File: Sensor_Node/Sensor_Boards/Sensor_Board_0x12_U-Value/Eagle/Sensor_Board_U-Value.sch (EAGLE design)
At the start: 25 parts, among them IC1 MCP3911A0-E/SS, IC2 4066D, J2 ARDUINO_ISP, U2 ATMEGA328P_TQFP, Y1 8MHZ

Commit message: Added WSN eagle library
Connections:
- removed net D11_MOSI: U2.PB3(MOSI/OC2)
- removed net D12_MISO: J2.MISO, J2.MOSI, U2.PB4(MISO)
- removed net D13_SCK: J2.SCK, U2.PB5(SCK)
- removed net N$16: U2.PD2(INT0)
- removed net N$20: U2.PD6(AIN0)
- removed net N$21: U2.PD7(AIN1)
- net ADCLK: now also U2.PD2(INT0)
- net AD_CS: now also U2.PD6(AIN0)
- net DATA_READY: now also U2.PD7(AIN1)
- net MISO: now also J2.MISO, U2.PB4(MISO)
- net MOSI: now also J2.MOSI, U2.PB3(MOSI/OC2)
- net SCK: now also J2.SCK, U2.PB5(SCK)
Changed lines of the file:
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@@
 <?xml version="1.0" encoding="utf-8"?>
 <!DOCTYPE eagle SYSTEM "eagle.dtd">
-<eagle version="7.6.0">
+<eagle version="8.2.2">
 <drawing>
 <settings>
@@
 <part name="NC10" library="wsn" deviceset="NC" device=""/>
 <part name="NC11" library="wsn" deviceset="NC" device=""/>
-<part name="NC12" library="wsn" deviceset="NC" device=""/>
 <part name="NC13" library="wsn" deviceset="NC" device=""/>
 <part name="NC14" library="wsn" deviceset="NC" device=""/>
 <part name="NC15" library="wsn" deviceset="NC" device=""/>
-<part name="NC16" library="wsn" deviceset="NC" device=""/>
-<part name="NC17" library="wsn" deviceset="NC" device=""/>
 <part name="NC18" library="wsn" deviceset="NC" device=""/>
 <part name="GND6" library="supply1" deviceset="GND" device=""/>
@@
 <instance part="NC10" gate="G$1" x="236.22" y="83.82"/>
 <instance part="NC11" gate="G$1" x="236.22" y="81.28"/>
-<instance part="NC12" gate="G$1" x="236.22" y="78.74"/>
 <instance part="NC13" gate="G$1" x="236.22" y="76.2"/>
 <instance part="NC14" gate="G$1" x="236.22" y="73.66"/>
 <instance part="NC15" gate="G$1" x="236.22" y="71.12"/>
-<instance part="NC16" gate="G$1" x="236.22" y="68.58"/>
-<instance part="NC17" gate="G$1" x="236.22" y="66.04"/>
 <instance part="NC18" gate="G$1" x="236.22" y="63.5"/>
 <instance part="GND6" gate="1" x="182.88" y="43.18"/>
@@
 <pinref part="IC1" gate="G$1" pin="SDO"/>
 </segment>
+<segment>
+<pinref part="U2" gate="U$1" pin="PB4(MISO)"/>
+<wire x1="236.22" y1="53.34" x2="233.68" y2="53.34" width="0.1524" layer="91"/>
+<label x="236.22" y="53.34" size="1.27" layer="95" xref="yes"/>
+</segment>
+<segment>
+<pinref part="J2" gate="G$1" pin="MISO"/>
+<wire x1="210.82" y1="137.16" x2="213.36" y2="137.16" width="0.1524" layer="91"/>
+<label x="213.36" y="137.16" size="1.27" layer="95" xref="yes"/>
+</segment>
 </net>
 <net name="MOSI" class="0">
@@
 <pinref part="IC1" gate="G$1" pin="SDI"/>
 </segment>
+<segment>
+<pinref part="U2" gate="U$1" pin="PB3(MOSI/OC2)"/>
+<wire x1="236.22" y1="55.88" x2="233.68" y2="55.88" width="0.1524" layer="91"/>
+<label x="236.22" y="55.88" size="1.27" layer="95" xref="yes"/>
+</segment>
+<segment>
+<pinref part="J2" gate="G$1" pin="MOSI"/>
+<wire x1="210.82" y1="142.24" x2="213.36" y2="142.24" width="0.1524" layer="91"/>
+<label x="213.36" y="142.24" size="1.27" layer="95" xref="yes"/>
+</segment>
 </net>
 <net name="SCK" class="0">
@@
 <pinref part="IC1" gate="G$1" pin="SCK"/>
 </segment>
+<segment>
+<pinref part="U2" gate="U$1" pin="PB5(SCK)"/>
+<wire x1="236.22" y1="50.8" x2="233.68" y2="50.8" width="0.1524" layer="91"/>
+<label x="236.22" y="50.8" size="1.27" layer="95" xref="yes"/>
+</segment>
+<segment>
+<pinref part="J2" gate="G$1" pin="SCK"/>
+<wire x1="210.82" y1="139.7" x2="213.36" y2="139.7" width="0.1524" layer="91"/>
+<label x="213.36" y="139.7" size="1.27" layer="95" xref="yes"/>
+</segment>
 </net>
 <net name="AD_RESET" class="0">
@@
 <label x="156.21" y="135.89" size="1.778" layer="95"/>
 <pinref part="IC1" gate="G$1" pin="/DR"/>
+</segment>
+<segment>
+<pinref part="U2" gate="U$1" pin="PD7(AIN1)"/>
+<wire x1="236.22" y1="66.04" x2="233.68" y2="66.04" width="0.1524" layer="91"/>
+<label x="236.22" y="66.04" size="1.27" layer="95" xref="yes"/>
 </segment>
 </net>
@@
 <pinref part="IC1" gate="G$1" pin="OSC1"/>
 </segment>
+<segment>
+<pinref part="U2" gate="U$1" pin="PD2(INT0)"/>
+<wire x1="236.22" y1="78.74" x2="233.68" y2="78.74" width="0.1524" layer="91"/>
+<label x="236.22" y="78.74" size="1.27" layer="95" xref="yes"/>
+</segment>
 </net>
 <net name="N$2" class="0">
@@
 <label x="156.21" y="132.08" size="1.778" layer="95"/>
 <pinref part="IC1" gate="G$1" pin="/CS"/>
+</segment>
+<segment>
+<pinref part="U2" gate="U$1" pin="PD6(AIN0)"/>
+<wire x1="236.22" y1="68.58" x2="233.68" y2="68.58" width="0.1524" layer="91"/>
+<label x="236.22" y="68.58" size="1.27" layer="95" xref="yes"/>
 </segment>
 </net>
@@
 </segment>
 </net>
-<net name="N$16" class="0">
-<segment>
-<pinref part="U2" gate="U$1" pin="PD2(INT0)"/>
-<wire x1="236.22" y1="78.74" x2="233.68" y2="78.74" width="0.1524" layer="91"/>
-</segment>
-</net>
 <net name="N$17" class="0">
 <segment>
@@
 <pinref part="U2" gate="U$1" pin="PD5(T1)"/>
 <wire x1="236.22" y1="71.12" x2="233.68" y2="71.12" width="0.1524" layer="91"/>
-</segment>
-</net>
-<net name="N$20" class="0">
-<segment>
-<pinref part="U2" gate="U$1" pin="PD6(AIN0)"/>
-<wire x1="236.22" y1="68.58" x2="233.68" y2="68.58" width="0.1524" layer="91"/>
-</segment>
-</net>
-<net name="N$21" class="0">
-<segment>
-<pinref part="U2" gate="U$1" pin="PD7(AIN1)"/>
-<wire x1="236.22" y1="66.04" x2="233.68" y2="66.04" width="0.1524" layer="91"/>
 </segment>
 </net>
@@
 </segment>
 </net>
-<net name="D11_MOSI" class="0">
-<segment>
-<pinref part="U2" gate="U$1" pin="PB3(MOSI/OC2)"/>
-<wire x1="236.22" y1="55.88" x2="233.68" y2="55.88" width="0.1524" layer="91"/>
-<label x="236.22" y="55.88" size="1.27" layer="95" xref="yes"/>
-</segment>
-</net>
-<net name="D12_MISO" class="0">
-<segment>
-<pinref part="U2" gate="U$1" pin="PB4(MISO)"/>
-<wire x1="236.22" y1="53.34" x2="233.68" y2="53.34" width="0.1524" layer="91"/>
-<label x="236.22" y="53.34" size="1.27" layer="95" xref="yes"/>
-</segment>
-<segment>
-<pinref part="J2" gate="G$1" pin="MOSI"/>
-<wire x1="210.82" y1="142.24" x2="213.36" y2="142.24" width="0.1524" layer="91"/>
-<label x="213.36" y="142.24" size="1.27" layer="95" xref="yes"/>
-</segment>
-<segment>
-<pinref part="J2" gate="G$1" pin="MISO"/>
-<wire x1="210.82" y1="137.16" x2="213.36" y2="137.16" width="0.1524" layer="91"/>
-<label x="213.36" y="137.16" size="1.27" layer="95" xref="yes"/>
-</segment>
-</net>
-<net name="D13_SCK" class="0">
-<segment>
-<pinref part="U2" gate="U$1" pin="PB5(SCK)"/>
-<wire x1="236.22" y1="50.8" x2="233.68" y2="50.8" width="0.1524" layer="91"/>
-<label x="236.22" y="50.8" size="1.27" layer="95" xref="yes"/>
-</segment>
-<segment>
-<pinref part="J2" gate="G$1" pin="SCK"/>
-<wire x1="210.82" y1="139.7" x2="213.36" y2="139.7" width="0.1524" layer="91"/>
-<label x="213.36" y="139.7" size="1.27" layer="95" xref="yes"/>
-</segment>
-</net>

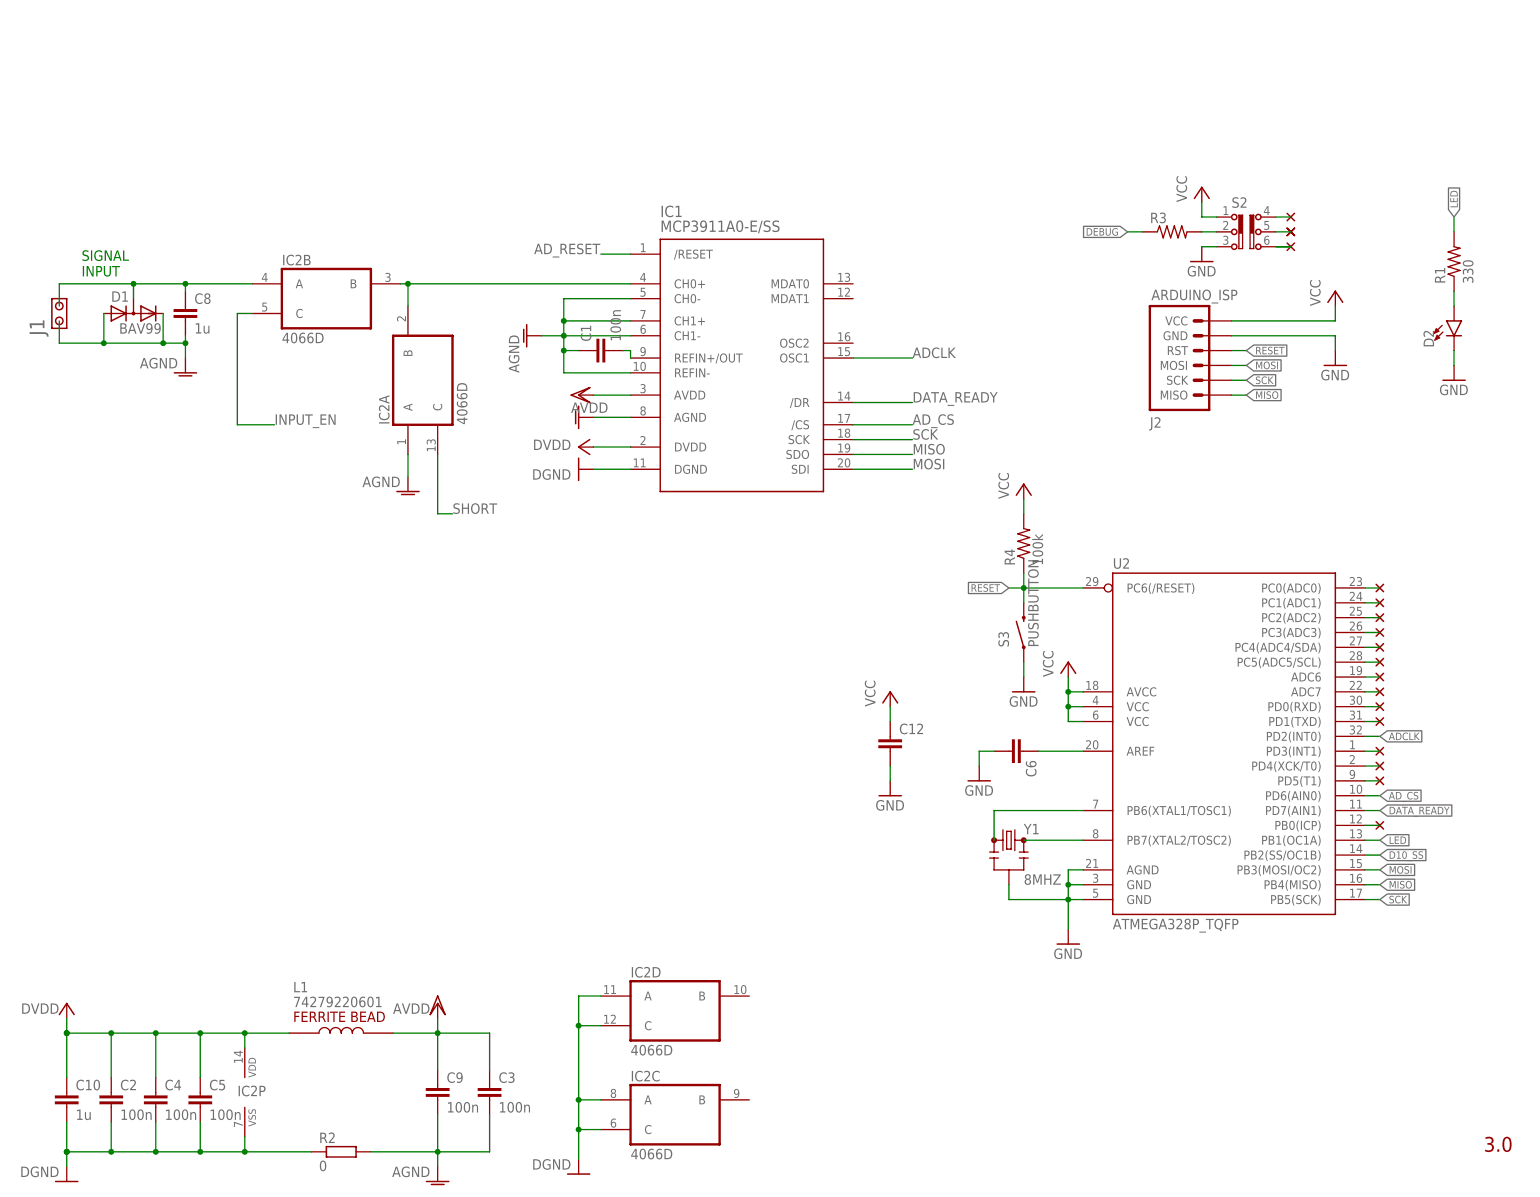
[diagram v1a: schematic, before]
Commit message: Update U-Value board, Added Readme for sensor boards
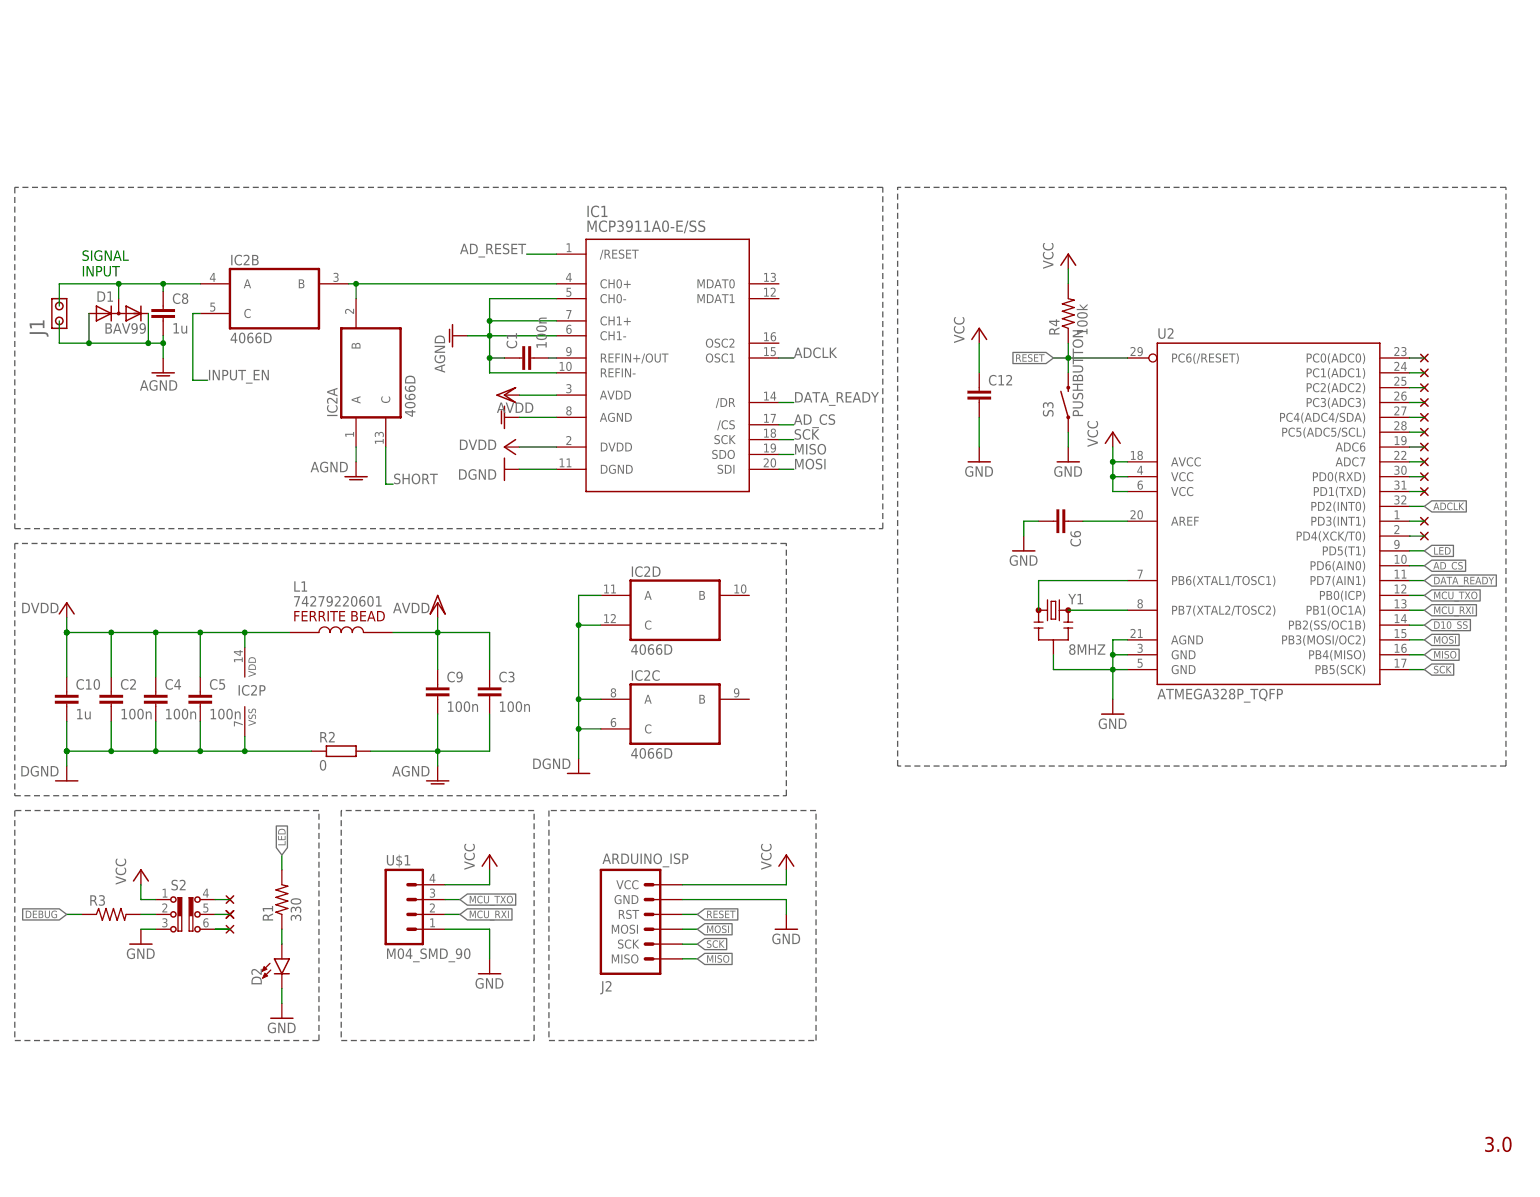
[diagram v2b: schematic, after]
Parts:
- added U$1: M04_SMD_90, wsn:M04_SMD_90
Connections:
- removed net N$19: U2.PD5(T1)
- removed net N$22: U2.PB0(ICP)
- new net MCU_RXI: U$1.2, U2.PB1(OC1A)
- new net MCU_TXO: U$1.3, U2.PB0(ICP)
- net GND: now also U$1.1
- net LED: now also U2.PD5(T1); no longer U2.PB1(OC1A)
- net VCC: now also U$1.4
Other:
- moved on the sheet: C1, C10, C12, C2, C3, C4, C5, C6, C8, C9, D1, D2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

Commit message: Updated gatway board, updated u-value board
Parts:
- removed R3: (no value), wsn:RESISTOR0805-RES
- removed S2: SLIDE_SWITCH_JS202011SCQN, wsn:SLIDE_SWITCH_JS202011SCQN
- added J4, J5: 1x3 RA Female .1", wsn:M03SMD_RA_FEMALE
- added R5, R6: 4.7K, wsn:RESISTOR0805-RES
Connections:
- net N$14 renamed FTDI_TXO
- net N$15 renamed FTDI_RXI
- removed net DEBUG: R3.1
- removed net N$1: S2.6
- removed net N$26: S2.4
- removed net N$28: U2.PC0(ADC0)
- removed net N$31: R3.2, S2.2
- removed net N$5: U2.PC1(ADC1)
- new net DS18B20_1: J4.2, R5.1, U2.PC0(ADC0)
- new net DS18B20_2: J5.2, R6.1, U2.PC1(ADC1)
- new net N$15: J4.1
- net GND: now also J5.1; no longer S2.3, U$1.1
- net MCU_RXI: now also U$1.3; no longer U$1.2
- net MCU_TXO: now also U$1.2; no longer U$1.3
- net N$4: now also U$1.4; no longer S2.5
- net VCC: now also J4.3, J5.3, R5.2, R6.2, U$1.1; no longer S2.1, U$1.4
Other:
- note added: "CommBoard Connector"
- note added: "Debugging"
- note added: "FTDI Connector"
- note added: "ISP Connector"
- note added: "Microcontroller"
- note added: "Separation Analog / Digital"
- note added: "Signal Acquisition"
- note added: "Temperature Sensors"
- note removed: "3.0"
- moved on the sheet: C1, C10, C12, C2, C3, C4, C5, C6, C8, C9, D1, D2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
